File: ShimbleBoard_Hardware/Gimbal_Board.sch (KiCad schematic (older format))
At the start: 54 parts, among them Q1 2N3904, Q2 2N3904, Q3 2N3904, Q4 2N3904, Q5 2N3904, Q6 2N3904, Q7 2N3904, Q8 2N3904, U1 TM4C129E_Launchpad, U2 OKI, U3 OKI

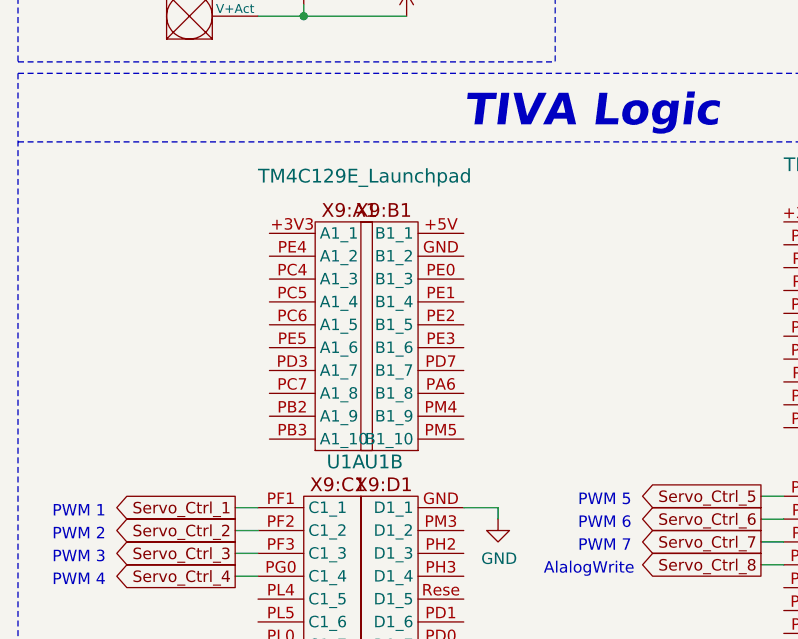
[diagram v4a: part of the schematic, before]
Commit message: BJT changes
BJT changed to surface mount
Minor re-wiring
Ground & +5VA plains changed to solid
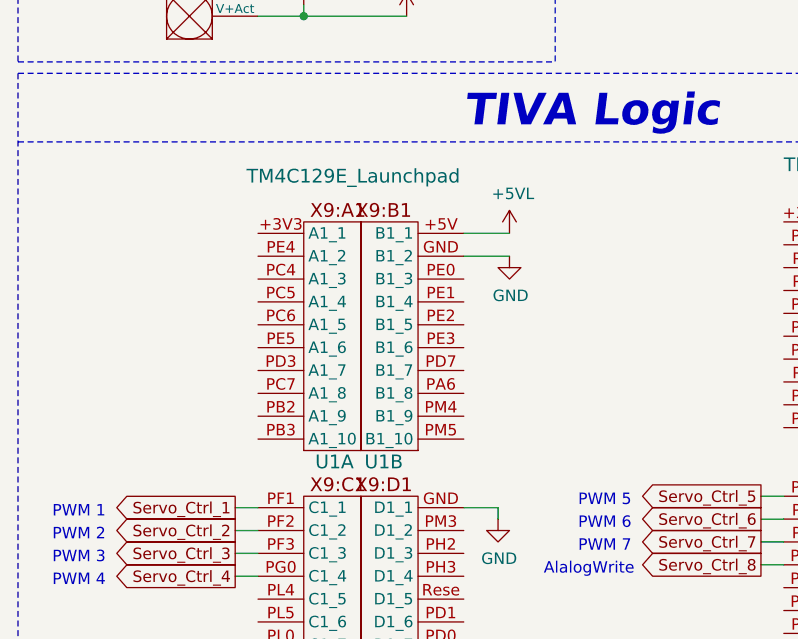
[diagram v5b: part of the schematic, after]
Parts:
- Q1, Q2, Q3, Q4, Q5, Q6, Q7, Q8: footprint Package_TO_SOT_THT:TO-92_Inline -> Package_TO_SOT_SMD:SOT-23_Handsoldering
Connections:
- net +5VL: now also U1.+5V (B1_1)
- net GND: now also U1.GND (B1_2)
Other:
- moved on the sheet: U1A
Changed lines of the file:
@@
 L MRDT_Shields:TM4C129E_Launchpad U1
 U 1 1 5DA28D2E
-P 1300 12100
-F 0 "U1" H 1350 12050 60  0000 L CNN
-F 1 "TM4C129E_Launchpad" H 1050 13300 60  0000 L CNN
-F 2 "MRDT_Shields:TM4C129E_Launchpad_FULL_THT_BOTTOM" H 1300 12100 60  0001 C CNN
-F 3 "" H 1300 12100 60  0001 C CNN
-	1    1300 12100
+P 1250 12100
+F 0 "U1" H 1300 12050 60  0000 L CNN
+F 1 "TM4C129E_Launchpad" H 1000 13300 60  0000 L CNN
+F 2 "MRDT_Shields:TM4C129E_Launchpad_FULL_THT_BOTTOM" H 1250 12100 60  0001 C CNN
+F 3 "" H 1250 12100 60  0001 C CNN
+	1    1250 12100
 	1    0    0    -1
 $EndComp
@@
 F 0 "Q7" H 10390 12846 50  0000 L CNN
 F 1 "2N3904" H 10390 12755 50  0000 L CNN
-F 2 "Package_TO_SOT_THT:TO-92_Inline" H 10400 12725 50  0001 L CIN
+F 2 "Package_TO_SOT_SMD:SOT-23_Handsoldering" H 10400 12725 50  0001 L CIN
 F 3 "https://www.fairchildsemi.com/datasheets/2N/2N3904.pdf" H 10200 12800 50  0001 L CNN
 	1    10200 12800
@@
 F 0 "Q8" H 11140 12846 50  0000 L CNN
 F 1 "2N3904" H 11140 12755 50  0000 L CNN
-F 2 "Package_TO_SOT_THT:TO-92_Inline" H 11150 12725 50  0001 L CIN
+F 2 "Package_TO_SOT_SMD:SOT-23_Handsoldering" H 11150 12725 50  0001 L CIN
 F 3 "https://www.fairchildsemi.com/datasheets/2N/2N3904.pdf" H 10950 12800 50  0001 L CNN
 	1    10950 12800
@@
 F 0 "Q1" H 5890 12846 50  0000 L CNN
 F 1 "2N3904" H 5890 12755 50  0000 L CNN
-F 2 "Package_TO_SOT_THT:TO-92_Inline" H 5900 12725 50  0001 L CIN
+F 2 "Package_TO_SOT_SMD:SOT-23_Handsoldering" H 5900 12725 50  0001 L CIN
 F 3 "https://www.fairchildsemi.com/datasheets/2N/2N3904.pdf" H 5700 12800 50  0001 L CNN
 	1    5700 12800
@@
 F 0 "Q2" H 6640 12846 50  0000 L CNN
 F 1 "2N3904" H 6640 12755 50  0000 L CNN
-F 2 "Package_TO_SOT_THT:TO-92_Inline" H 6650 12725 50  0001 L CIN
+F 2 "Package_TO_SOT_SMD:SOT-23_Handsoldering" H 6650 12725 50  0001 L CIN
 F 3 "https://www.fairchildsemi.com/datasheets/2N/2N3904.pdf" H 6450 12800 50  0001 L CNN
 	1    6450 12800
@@
 F 0 "Q3" H 7390 12846 50  0000 L CNN
 F 1 "2N3904" H 7390 12755 50  0000 L CNN
-F 2 "Package_TO_SOT_THT:TO-92_Inline" H 7400 12725 50  0001 L CIN
+F 2 "Package_TO_SOT_SMD:SOT-23_Handsoldering" H 7400 12725 50  0001 L CIN
 F 3 "https://www.fairchildsemi.com/datasheets/2N/2N3904.pdf" H 7200 12800 50  0001 L CNN
 	1    7200 12800
@@
 F 0 "Q4" H 8140 12846 50  0000 L CNN
 F 1 "2N3904" H 8140 12755 50  0000 L CNN
-F 2 "Package_TO_SOT_THT:TO-92_Inline" H 8150 12725 50  0001 L CIN
+F 2 "Package_TO_SOT_SMD:SOT-23_Handsoldering" H 8150 12725 50  0001 L CIN
 F 3 "https://www.fairchildsemi.com/datasheets/2N/2N3904.pdf" H 7950 12800 50  0001 L CNN
 	1    7950 12800
@@
 F 0 "Q5" H 8890 12846 50  0000 L CNN
 F 1 "2N3904" H 8890 12755 50  0000 L CNN
-F 2 "Package_TO_SOT_THT:TO-92_Inline" H 8900 12725 50  0001 L CIN
+F 2 "Package_TO_SOT_SMD:SOT-23_Handsoldering" H 8900 12725 50  0001 L CIN
 F 3 "https://www.fairchildsemi.com/datasheets/2N/2N3904.pdf" H 8700 12800 50  0001 L CNN
 	1    8700 12800
@@
 F 0 "Q6" H 9640 12846 50  0000 L CNN
 F 1 "2N3904" H 9640 12755 50  0000 L CNN
-F 2 "Package_TO_SOT_THT:TO-92_Inline" H 9650 12725 50  0001 L CIN
+F 2 "Package_TO_SOT_SMD:SOT-23_Handsoldering" H 9650 12725 50  0001 L CIN
 F 3 "https://www.fairchildsemi.com/datasheets/2N/2N3904.pdf" H 9450 12800 50  0001 L CNN
 	1    9450 12800
@@
 Wire Notes Line
 	0    10750 4600 10750
+$Comp
+L power:GND #PWR0108
+U 1 1 5DA29F38
+P 2150 11250
+F 0 "#PWR0108" H 2150 11000 50  0001 C CNN
+F 1 "GND" H 2155 11077 50  0000 C CNN
+F 2 "" H 2150 11250 50  0001 C CNN
+F 3 "" H 2150 11250 50  0001 C CNN
+	1    2150 11250
+	1    0    0    -1
+$EndComp
+Wire Wire Line
+	2150 11250 1950 11250
+$Comp
+L power:+5VL #PWR0109
+U 1 1 5DA29F3F
+P 2150 11150
+F 0 "#PWR0109" H 2150 11000 50  0001 C CNN
+F 1 "+5VL" H 2165 11323 50  0000 C CNN
+F 2 "" H 2150 11150 50  0001 C CNN
+F 3 "" H 2150 11150 50  0001 C CNN
+	1    2150 11150
+	1    0    0    -1
+$EndComp
+Wire Wire Line
+	2150 11150 1950 11150
 $EndSCHEMATC

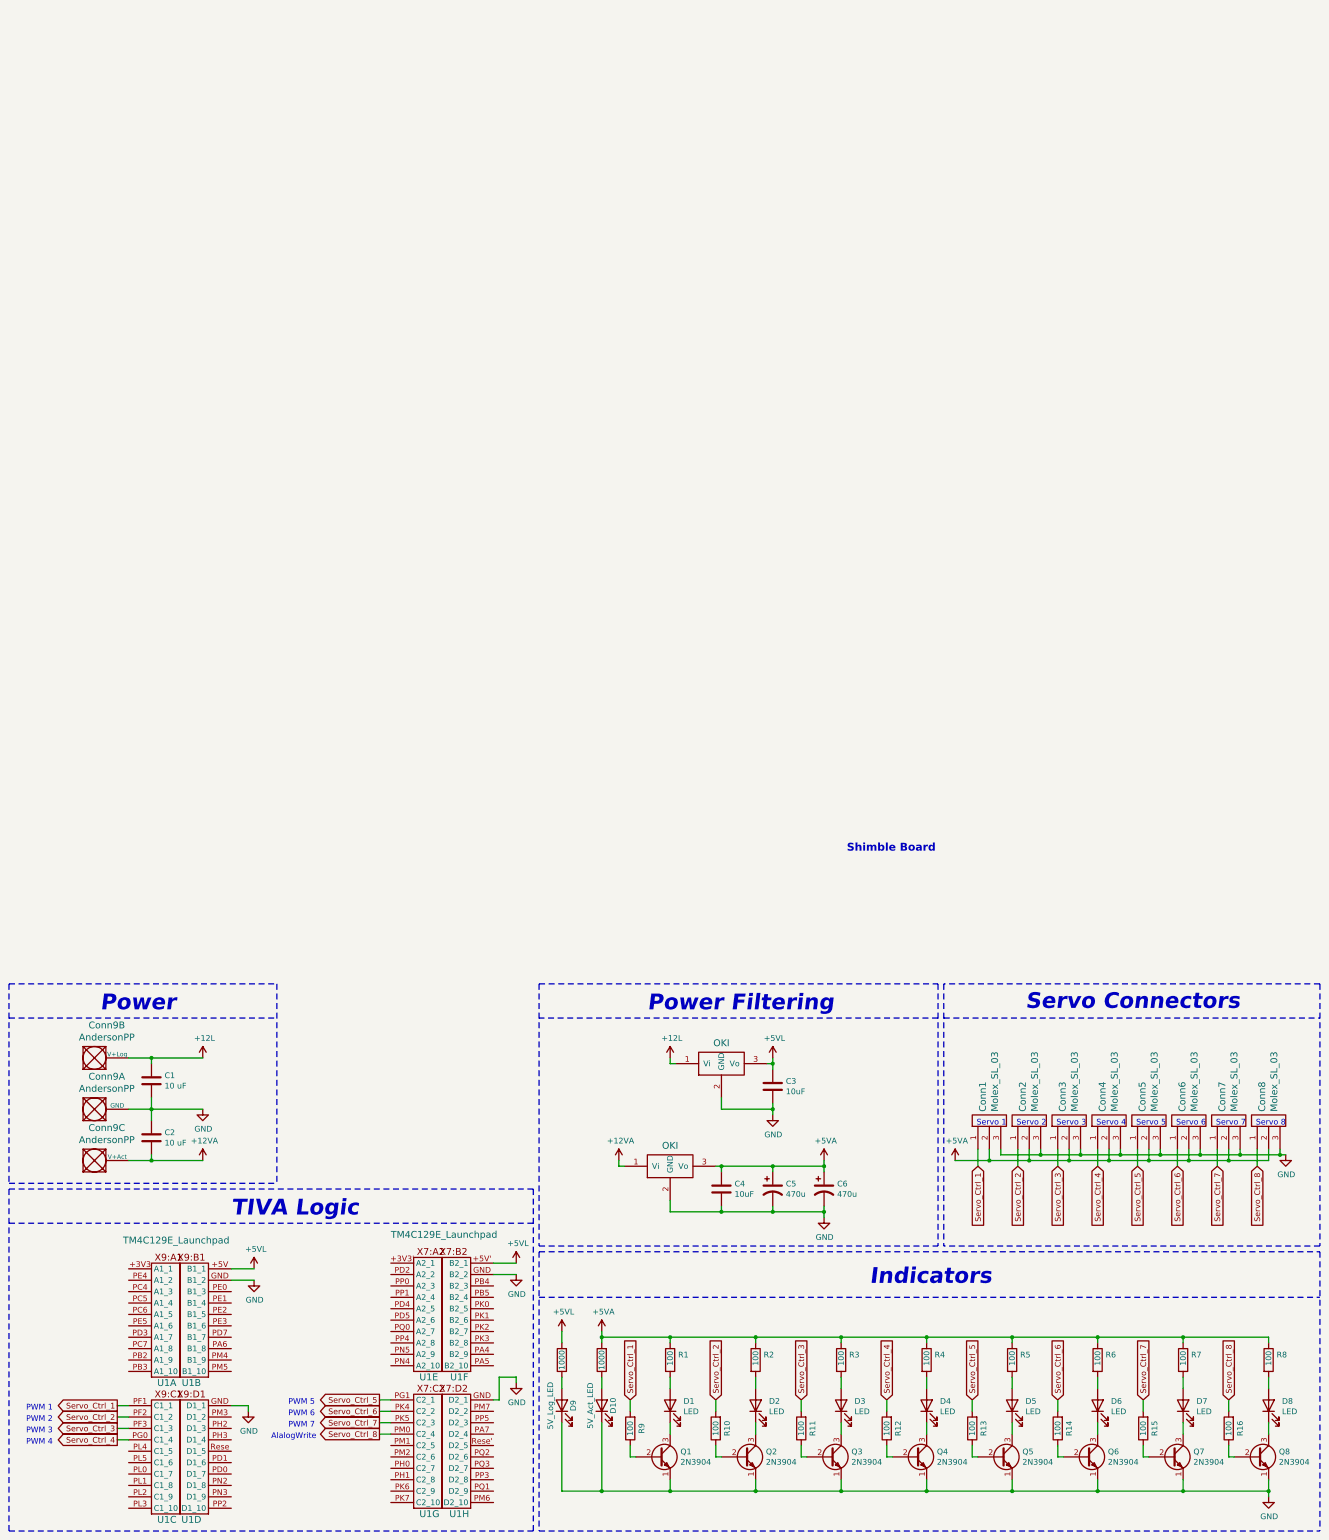
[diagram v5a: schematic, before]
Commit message: Resistor Changes
Resistors changed to 500 standard
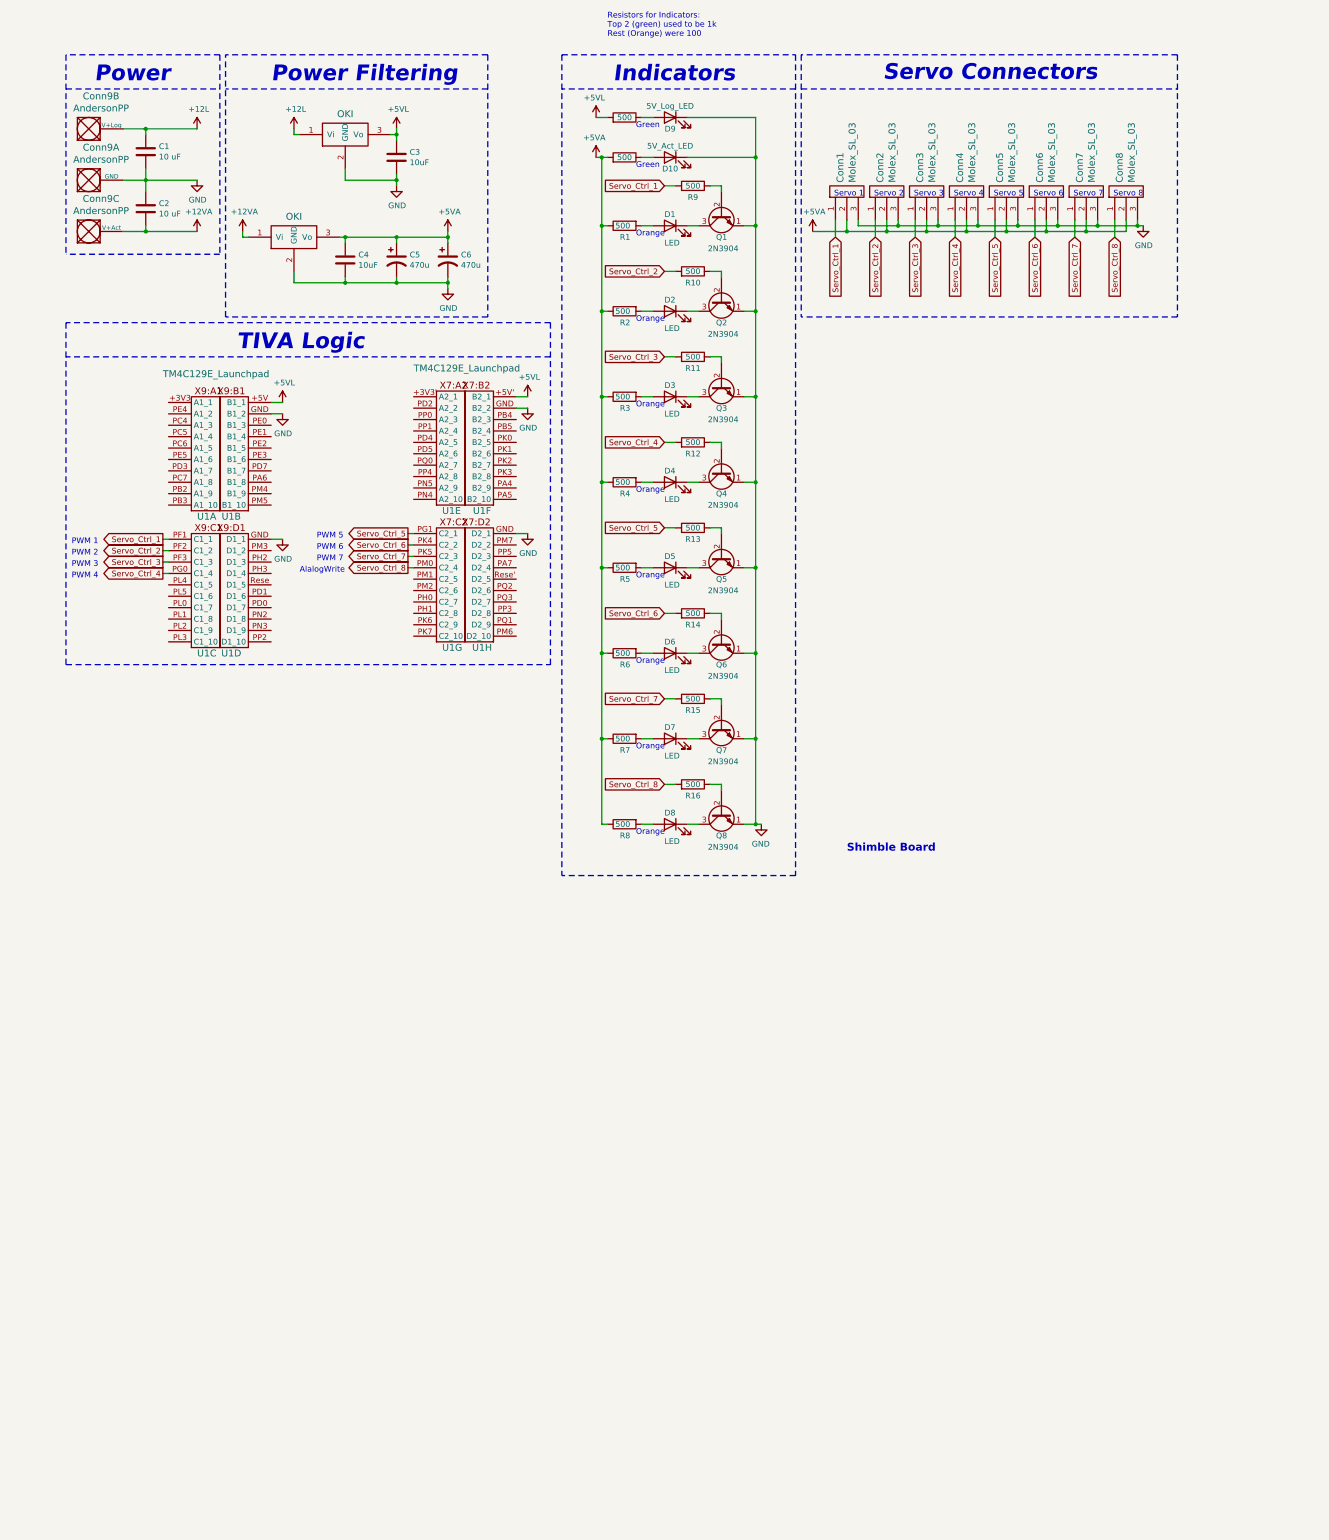
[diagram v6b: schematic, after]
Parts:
- R1, R10, R11, R12, R13, R14, R15, R16, R2, R3, R4, R5, R6, R7, R8, R9: value 100 -> 500
- R17, R18: value 1000 -> 500
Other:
- note added: "Green"
- note added: "Orange"
- note added: "Resistors for Indicators:\nTop 2 (green) used to be 1k\nRest (Orange) were 100"
- moved on the sheet: C1, C2, C3, C4, C5, C6, Conn1, Conn2, Conn3, Conn4, Conn5, Conn6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

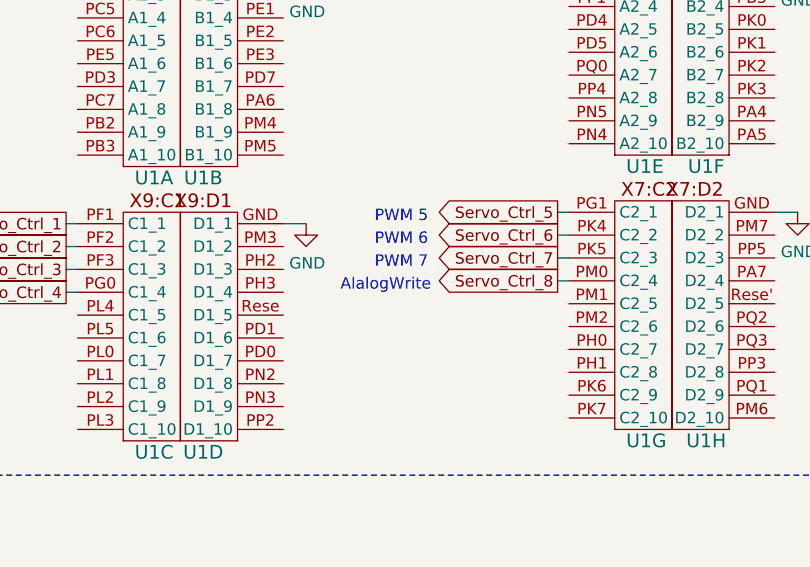
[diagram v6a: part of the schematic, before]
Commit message: Minor text change
AnalogWrite
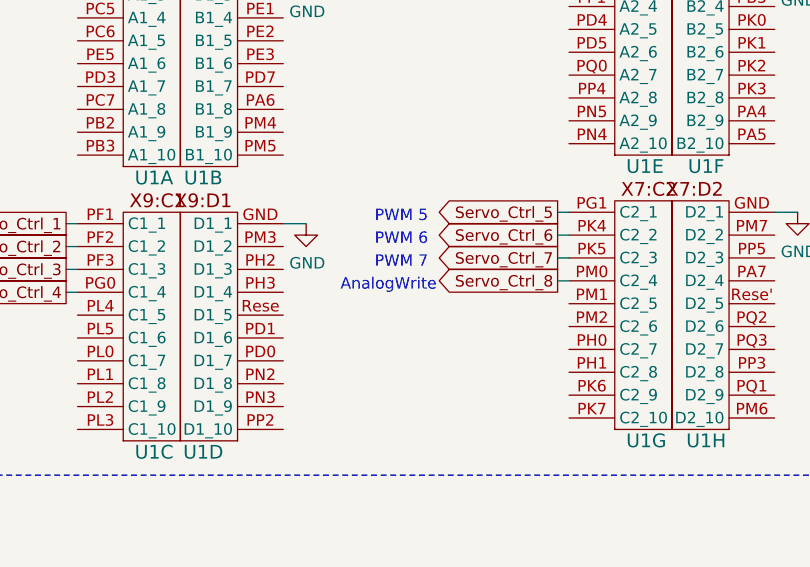
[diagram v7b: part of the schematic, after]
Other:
- note added: "AnalogWrite"
- note removed: "AlalogWrite"
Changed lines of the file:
@@
 PWM 5
 Text Notes 2550 5050 0    50   ~ 0
-AlalogWrite
+AnalogWrite
 Text GLabel 3500 4800 0    50   Output ~ 0
 Servo_Ctrl_6

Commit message: Major Overhaull
BJTs replaced by N-MOSFET
Buttons & switch added
PCB layout worked on (still not complete)
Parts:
- removed Q1, Q2, Q3, Q4, Q5, Q6, Q7, Q8: 2N3904, Package_TO_SOT_SMD:SOT-23_Handsoldering, symbol Transistor_BJT:2N3904
- added D10, D11, D12, D13, D14, D15, D16, D17, D18, D9: LED, Diode_SMD:D_0603_1608Metric_Pad1.05x0.95mm_HandSolder, symbol Device:LED
- added Q1, Q2, Q3, Q4, Q5, Q6, Q7, Q8: Q_NMOS_GDS, Package_TO_SOT_SMD:SOT-23_Handsoldering, symbol Device:Q_NMOS_GDS
- added R17, R18, R19, R20, R21, R22, R23, R24, R25, R26: 500, Resistor_SMD:R_0603_1608Metric_Pad1.05x0.95mm_HandSolder, symbol Device:R
- added SW1, SW2, SW3, SW4, SW5, SW6, SW7, SW8, SW9: SW_Push, Button_Switch_SMD:SW_SPST_TL3305A, symbol Switch:SW_Push
- added SW10: SW_SPDT, Button_Switch_THT:SW_CuK_OS102011MA1QN1_SPDT_Angled, symbol Switch:SW_SPDT
- renumbered D10 to D19, D9 to D20, R17 to R27, R18 to R28
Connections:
- net GND: now also D10.1 (K), D11.1 (K), D12.1 (K), D13.1 (K), D14.1 (K), D15.1 (K), D16.1 (K), D18.1 (K), D9.1 (K), Q1.2 (D), Q2.2 (D), Q3.2 (D), Q4.2 (D), Q5.2 (D), Q6.2 (D), Q7.2 (D), Q8.2 (D)
- net at R10.1: now also Q2.1 (G)
- net at D2.1 (K): now also Q2.3 (S)
- net at R11.1: now also Q3.1 (G)
- net at D3.1 (K): now also Q3.3 (S)
- net at R12.1: now also Q4.1 (G)
- net at D4.1 (K): now also Q4.3 (S)
- net at D8.1 (K): now also Q8.3 (S)
- net at R16.1: now also Q8.1 (G)
- net at D7.1 (K): now also Q7.3 (S)
- net at R15.1: now also Q7.1 (G)
- net at R9.1: now also Q1.1 (G)
- net at D1.1 (K): now also Q1.3 (S)
- net at R13.1: now also Q5.1 (G)
- net at D5.1 (K): now also Q5.3 (S)
- net at R14.1: now also Q6.1 (G)
- net at D6.1 (K): now also Q6.3 (S)
- net +3V3: now reaches U1.+3V3' (A2_1)
- net +3V3: now also U1.+3V3 (A1_1), SW1.1, SW10.2 (B), SW2.1, SW3.1, SW4.1, SW5.1, SW6.1, SW7.1, SW8.1, SW9.1
- net All_Servo_SW: now reaches U1.PD2 (A2_2)
- net All_Servo_SW: now also R26.1, SW10.3 (C)
- net Servo_SW_6: now reaches U1.PN4 (A2_10)
- net Servo_SW_6: now also R22.1, SW6.2
- net Servo_SW_5: now reaches U1.PN5 (A2_9)
- net Servo_SW_5: now also R21.1, SW5.2
- net Servo_SW_1: now reaches U1.PP0 (A2_3)
- net Servo_SW_1: now also R17.1, SW1.2
- net Servo_SW_2: now reaches U1.PP1 (A2_4)
- net Servo_SW_2: now also R18.1, SW2.2
- net Servo_SW_4: now reaches U1.PP4 (A2_8)
- net Servo_SW_4: now also R20.1, SW4.2
- net Servo_SW_3: now reaches U1.PQ0 (A2_7)
- net Servo_SW_3: now also R19.1, SW3.2
- net Servo_SW_7: now reaches U1.PK1 (B2_6)
- net Servo_SW_7: now also R23.1, SW7.2
- net Servo_SW_8: now reaches U1.PK2 (B2_7)
- net Servo_SW_8: now also R24.1, SW8.2
- net Servo_Setup_SW: now reaches U1.PK3 (B2_8)
- net Servo_Setup_SW: now also R25.1, SW9.2
- new net: D9.2 (A), R17.2
- new net: D10.2 (A), R18.2
- new net: D11.2 (A), R19.2
- new net: D12.2 (A), R20.2
- new net: D13.2 (A), R21.2
- new net: D14.2 (A), R22.2
- new net: D15.2 (A), R23.2
- new net: D16.2 (A), R24.2
- new net: D17.2 (A), R25.2
- new net: D18.2 (A), R26.2
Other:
- moved on the sheet: D1, D19, D2, D20, D3, D4, D5, D6, D7, D8, R1, R10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
